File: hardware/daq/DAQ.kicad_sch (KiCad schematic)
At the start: 175 parts, among them J1 ICD15S13E4GX00LF, J2 ICD15S13E4GX00LF, J3 ICD15S13E4GX00LF, J4 ICD15S13E4GX00LF, P1 0022272021, U1 ADS124S08IRHBT, U11 SN74AHCT125RGYR, U2 ADS124S08IRHBT, U3 LT6654BMPS6-5-TRMPBF, U4 LM1086IS-5.0_NOPB, U5 TPS73801DCQR, U6 TPSM63603RDHR, U7 TPSM63603RDHR, U8 TPSM63603RDHR, U9 ADS124S08IRHBT

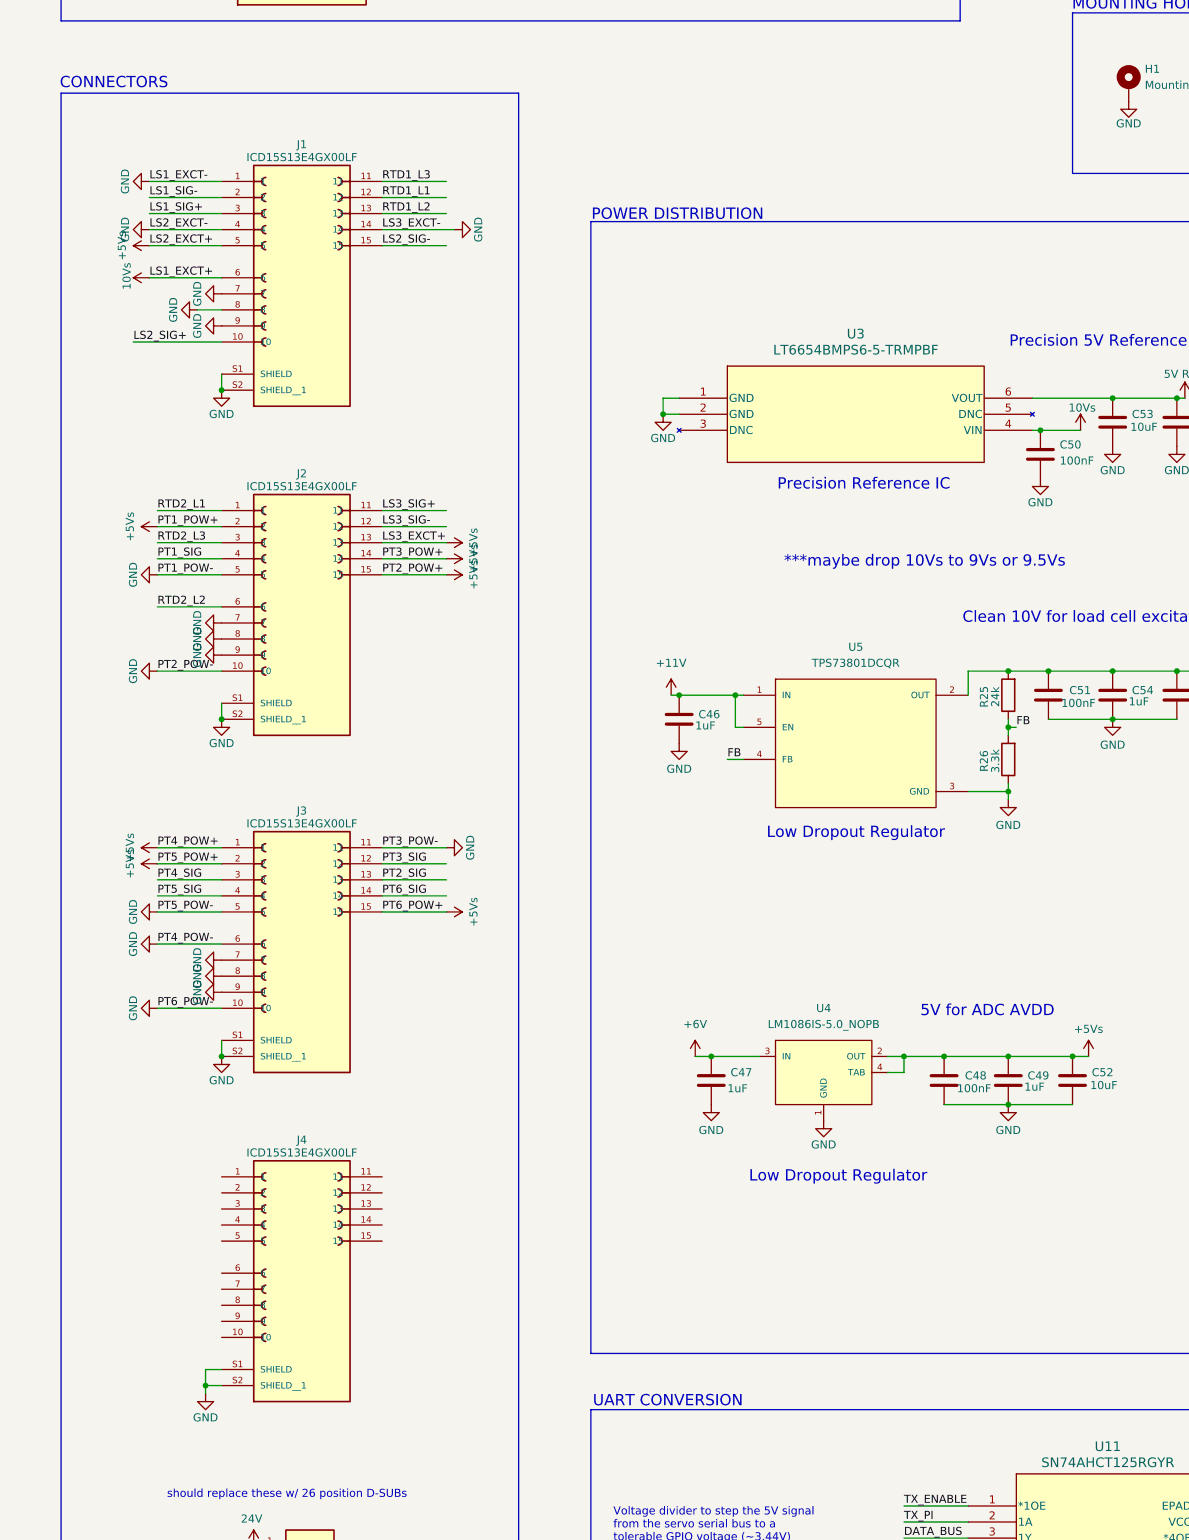
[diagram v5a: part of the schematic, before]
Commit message: starting to place 3rd ADC components
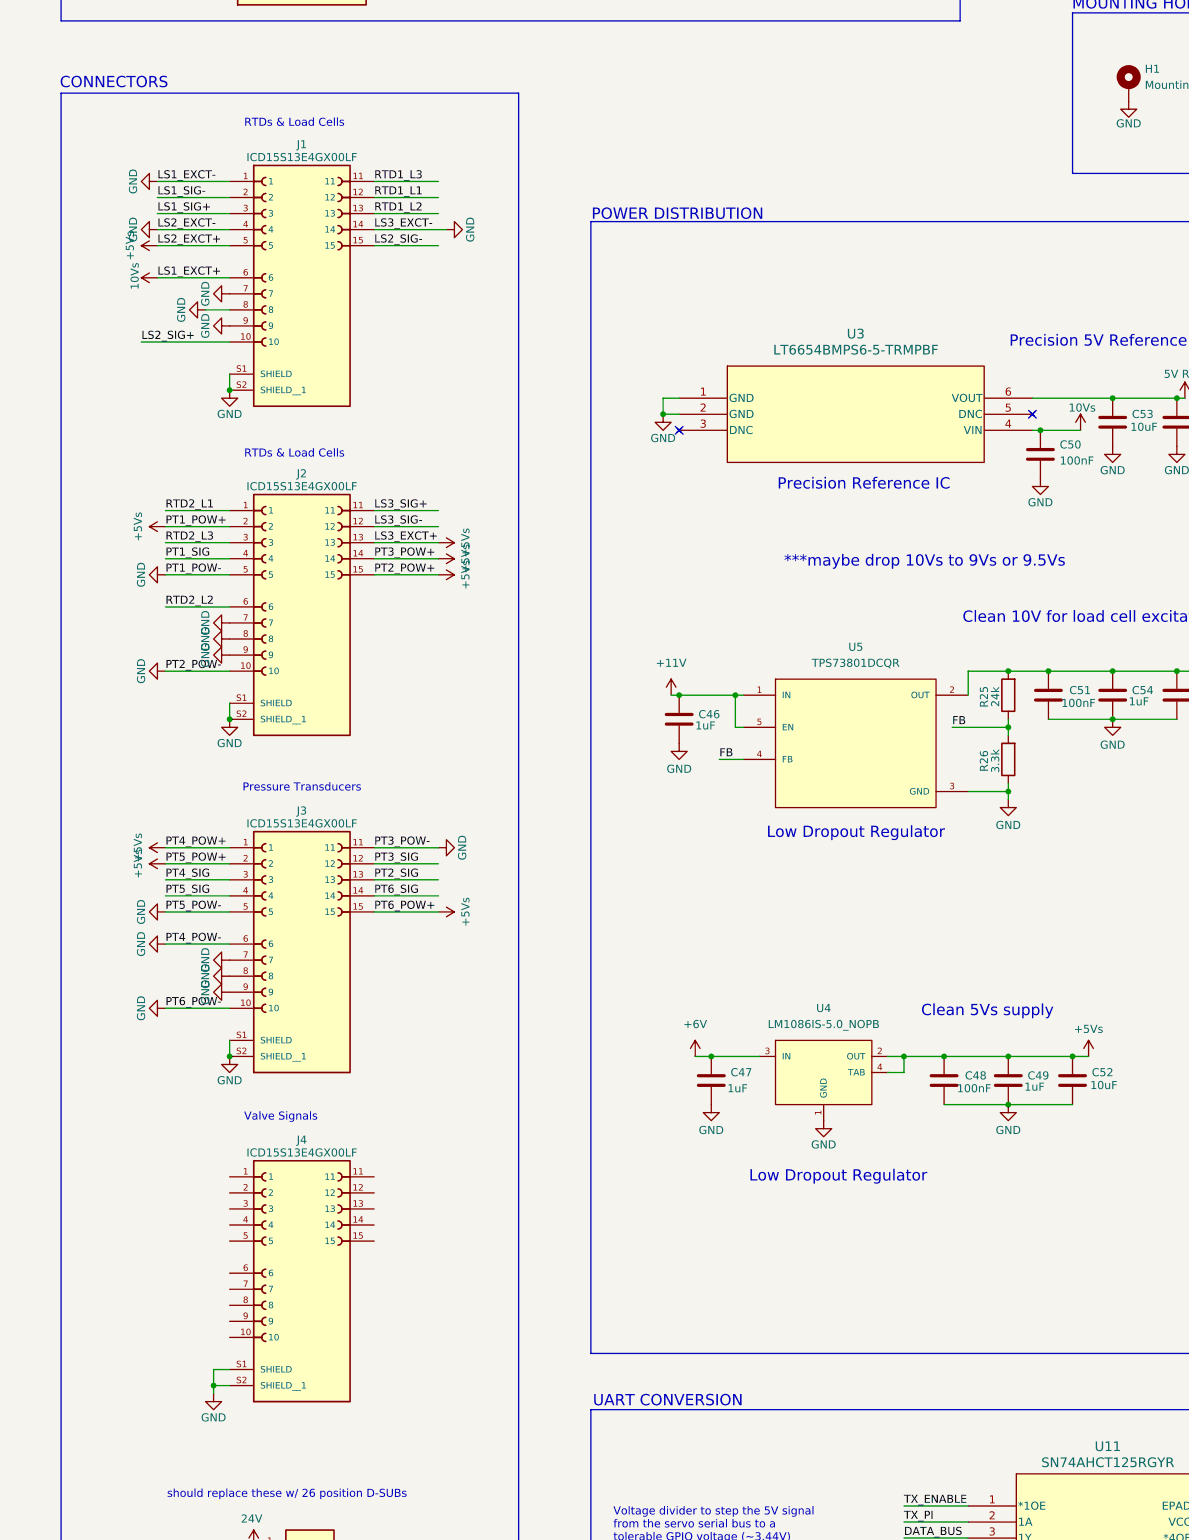
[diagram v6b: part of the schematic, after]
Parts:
- J2, J3, J4: footprint ICD15S13:AMPHENOL_ICD15S13E4GX00LF -> ICD15S13E4GX00LF:AMPHENOL_ICD15S13E4GX00LF
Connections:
- no-connect marks 28 -> 30
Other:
- note added: "Clean 5Vs supply"
- note added: "Pressure Transducers"
- note added: "RTDs & Load Cells"
- note added: "Valve Signals"
- note removed: "5V for ADC AVDD"

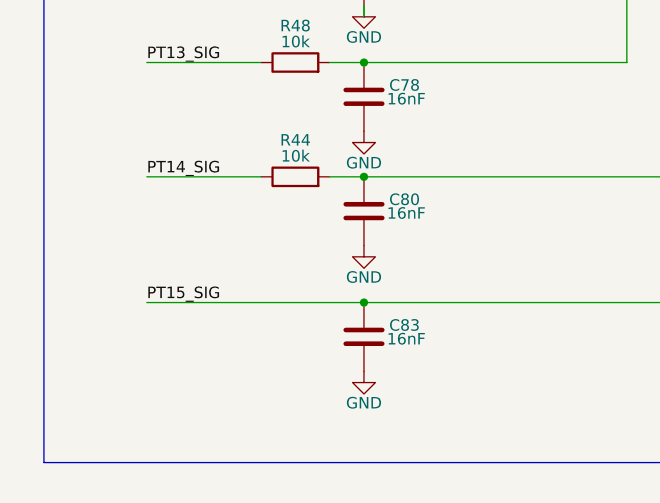
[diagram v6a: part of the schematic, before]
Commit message: last commit before redoing dsub pinouts
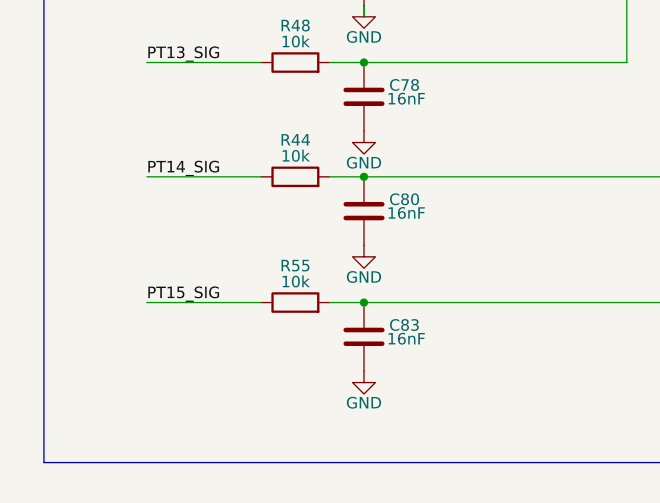
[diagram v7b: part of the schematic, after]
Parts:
- added R55: 10k, Resistor_SMD:R_0603_1608Metric, symbol Device:R
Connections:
- net PT15_SIG: now also R55.1; no longer C83.1, U9.22 (GPIO0_AIN8)
- new net: C83.1, R55.2, U9.22 (GPIO0_AIN8)
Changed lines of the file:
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@@
 	(wire
 		(pts
+			(xy 63.5 377.19) (xy 67.31 377.19)
+		)
+		(stroke
+			(width 0)
+			(type default)
+		)
+	)
+	(wire
+		(pts
 			(xy 448.31 365.76) (xy 454.66 365.76)
 		)
@@
 	(wire
 		(pts
-			(xy 43.18 377.19) (xy 67.31 377.19)
+			(xy 43.18 377.19) (xy 55.88 377.19)
 		)
 		(stroke
@@
 					(unit 1)
 				)
+			)
+		)
+	)
+	(symbol
+		(lib_id "Device:R")
+		(at 59.69 377.19 90)
+		(unit 1)
+		(exclude_from_sim no)
+		(in_bom yes)
+		(on_board yes)
+		(dnp no)
+		(property "Reference" "R55"
+			(at 59.69 373.126 90)
+			(effects
+				(font
+					(size 1.27 1.27)
+				)
+			)
+		)
+		(property "Value" "10k"
+			(at 59.69 374.904 90)
+			(effects
+				(font
+					(size 1.27 1.27)
+				)
+			)
+		)
+		(property "Footprint" "Resistor_SMD:R_0603_1608Metric"
+			(at 59.69 378.968 90)
+			(effects
+				(font
+					(size 1.27 1.27)
+				)
+				(hide yes)
+			)
+		)
+		(property "Datasheet" "~"
+			(at 59.69 377.19 0)
+			(effects
+				(font
+					(size 1.27 1.27)
+				)
+				(hide yes)
+			)
+		)
+		(property "Description" "Resistor"
+			(at 59.69 377.19 0)
+			(effects
+				(font
+					(size 1.27 1.27)
+				)
+				(hide yes)
+			)
+		)
+		(pin "1"
+		)
+		(pin "2"
+		)
+		(instances
+			(project "DAQ"
+				(path "/98ce85a8-ddff-4ecb-9668-dd271ba07a43"
+					(reference "R55")
+					(unit 1)
+				)

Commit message: re-mapped all DSUB pins
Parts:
- removed J3: ICD15S13E4GX00LF, ICD15S13E4GX00LF:AMPHENOL_ICD15S13E4GX00LF, symbol ICD15S13E4GX00LF:ICD15S13E4GX00LF
- added J1, J2, J3: ICD26S13E4GX00LF, ICD26S13E4GX00LF:AMPHENOL_ICD26S13E4GX00LF, symbol ICD26S13E4GX00LF:ICD26S13E4GX00LF
- J2, J4: footprint ICD15S13E4GX00LF:AMPHENOL_ICD15S13E4GX00LF -> ICD15S13:AMPHENOL_ICD15S13E4GX00LF
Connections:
- net +5Vs: now also J1.10, J1.15, J2.5, J4.10, J4.15, J4.5, J1.18, J2.18, J2.26, J3.18, J3.26; no longer D1.6, D2.4, D2.6, D3.4, D3.6, D4.4, D5.6, D6.4, J2.13, J2.14, J2.2
- net 10Vs: now also J2.10, J1.26; no longer J1.6
- net GND: now also J4.7, J4.8, J4.9, J1.1, J1.10, J1.19, J1.SH1 (SHIELD), J1.SH2 (SHIELD__1), J2.1, J2.10, J2.19, J2.SH1 (SHIELD), J2.SH2 (SHIELD__1), J3.1, J3.10, J3.19, J3.SH1 (SHIELD), J3.SH2 (SHIELD__1); no longer J1.1, J1.14, J1.4, J2.10, J2.5
- net IDAC2_1: now also J1.3, J1.12; no longer J1.13
- net IDAC2_2: now also J1.11, J1.15; no longer J2.6
- net LS1_SIG+: now also J2.2, J1.3; no longer J1.3
- net LS1_SIG-: now also J2.1, J1.2; no longer J1.2
- net LS2_SIG+: now also J2.3, J1.5; no longer J1.10
- net LS2_SIG-: now also J2.4, J1.4; no longer J1.15
- net LS3_SIG+: now also J2.6, J1.7; no longer J2.11
- net LS3_SIG-: now also J2.11, J1.6; no longer J2.12
- net PT10_SIG: now also J4.4
- net PT11_SIG: now also J4.6
- net PT12_SIG: now also J4.11
- net PT13_SIG: now also J4.12
- net PT14_SIG: now also J4.13
- net PT15_SIG: now also J4.14
- net PT1_SIG: now also J1.4; no longer J2.4
- net PT2_SIG: now also J1.6
- net PT3_SIG: now also J1.14
- net PT4_SIG: now also J2.12
- net PT5_SIG: now also J2.13
- net PT6_SIG: now also J2.14
- net PT7_SIG: now also J4.1
- net PT8_SIG: now also J4.2
- net PT9_SIG: now also J4.3
- net RTD1_L1: now also J1.2, J1.11; no longer J1.12
- net RTD1_L3: now also J1.1, J1.13; no longer J1.11
- net RTD2_L1: now also J1.13, J1.14; no longer J2.1
- net RTD2_L3: now also J1.12, J1.16; no longer J2.3
- new net LS2_EXCT+: D6.4
- new net LS3_EXCT+: D5.6
- new net PT1_POW+: D4.4
- new net PT2_POW+: D3.6
- new net PT3_POW+: D3.4
- new net PT4_POW+: D2.6
- new net PT5_POW+: D2.4
- new net PT6_POW+: D1.6
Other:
- note added: "Load Cells & PTs"
- note added: "PTs"
- note added: "RTDs & PTs"
- note removed: "Pressure Transducers"
- note removed: "Valve Signals"
- note removed: "add fuze"
- note removed: "should replace these w/ 26 position D-SUBs"
- moved on the sheet: C46, C47, C48, C49, C50, C51, C52, C53, C54, C55, C56, C57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
